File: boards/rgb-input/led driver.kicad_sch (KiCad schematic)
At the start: 4 parts, among them U6 TLC5947DAP

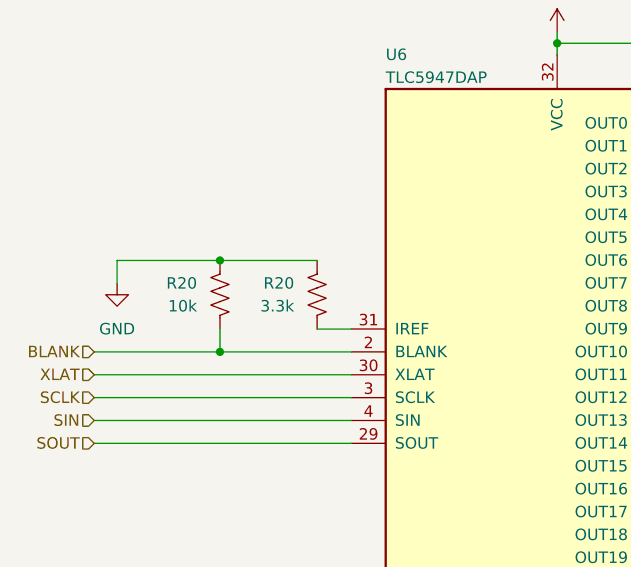
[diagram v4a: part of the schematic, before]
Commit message: routed the rgb setup
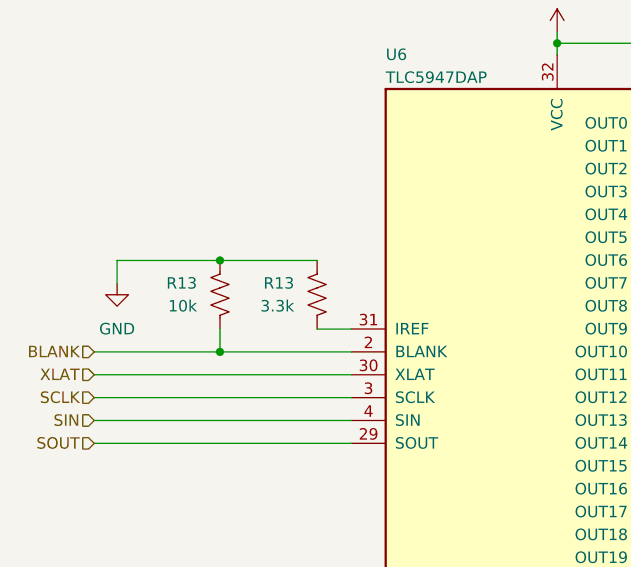
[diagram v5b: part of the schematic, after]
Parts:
- renumbered R20 to R13
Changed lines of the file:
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@@
   (symbol (lib_id "Device:R_US") (at 95.25 80.01 0) (mirror x) (unit 1)
     (in_bom yes) (on_board yes) (dnp no) (fields_autoplaced)
-    (property "Reference" "R20" (at 92.71 78.74 0)
+    (property "Reference" "R13" (at 92.71 78.74 0)
       (effects (font (size 1.27 1.27)) (justify right))
     )
@@
     (instances
       (project "rgb-input"
+        (path "/c83c6236-96e9-46ad-9d7a-9e2efa4a7966/802175d5-fb4b-4457-a117-b0f397189ff7"
+          (reference "R13") (unit 1)
+        )
+        (path "/c83c6236-96e9-46ad-9d7a-9e2efa4a7966/846833bc-7ec6-4ec6-86e7-310fef01b65c/1a23e144-e8e8-4225-b5a6-d9d839ced076"
+          (reference "R46") (unit 1)
+        )
+        (path "/c83c6236-96e9-46ad-9d7a-9e2efa4a7966/846833bc-7ec6-4ec6-86e7-310fef01b65c/720a8c4a-525c-4eec-8216-6ac4d044fce4"
+          (reference "R48") (unit 1)
+        )
+        (path "/c83c6236-96e9-46ad-9d7a-9e2efa4a7966/76149826-8526-4a6c-8e11-6dc0109cc281"
+          (reference "R26") (unit 1)
+        )
+        (path "/c83c6236-96e9-46ad-9d7a-9e2efa4a7966/d24c7443-0875-4d8e-b56e-81b211cd6f3d"
+          (reference "R25") (unit 1)
+        )
+        (path "/c83c6236-96e9-46ad-9d7a-9e2efa4a7966/7fda9512-7a31-4b6e-85db-2478bfe7f375"
+          (reference "R24") (unit 1)
+        )
+        (path "/c83c6236-96e9-46ad-9d7a-9e2efa4a7966/597c781a-3a73-4808-b6ed-8c917478e623"
+          (reference "R23") (unit 1)
+        )
+        (path "/c83c6236-96e9-46ad-9d7a-9e2efa4a7966/1ca70e91-4481-4c96-8c08-39dd142498e5"
+          (reference "R22") (unit 1)
+        )
+        (path "/c83c6236-96e9-46ad-9d7a-9e2efa4a7966/c9e1b2da-9064-45a5-a0a2-ee072f7e1acf"
+          (reference "R21") (unit 1)
+        )
+        (path "/c83c6236-96e9-46ad-9d7a-9e2efa4a7966/ef548cdc-9d5d-4f8e-8f54-0c2e96dbe3f0"
+          (reference "R1") (unit 1)
+        )
         (path "/c83c6236-96e9-46ad-9d7a-9e2efa4a7966/120468c6-3bec-414c-9049-57af589f397a"
           (reference "R20") (unit 1)
-        )
-        (path "/c83c6236-96e9-46ad-9d7a-9e2efa4a7966/846833bc-7ec6-4ec6-86e7-310fef01b65c/1a23e144-e8e8-4225-b5a6-d9d839ced076"
-          (reference "R46") (unit 1)
-        )
-        (path "/c83c6236-96e9-46ad-9d7a-9e2efa4a7966/846833bc-7ec6-4ec6-86e7-310fef01b65c/720a8c4a-525c-4eec-8216-6ac4d044fce4"
-          (reference "R48") (unit 1)
-        )
-        (path "/c83c6236-96e9-46ad-9d7a-9e2efa4a7966/76149826-8526-4a6c-8e11-6dc0109cc281"
-          (reference "R26") (unit 1)
-        )
-        (path "/c83c6236-96e9-46ad-9d7a-9e2efa4a7966/d24c7443-0875-4d8e-b56e-81b211cd6f3d"
-          (reference "R25") (unit 1)
-        )
-        (path "/c83c6236-96e9-46ad-9d7a-9e2efa4a7966/7fda9512-7a31-4b6e-85db-2478bfe7f375"
-          (reference "R24") (unit 1)
-        )
-        (path "/c83c6236-96e9-46ad-9d7a-9e2efa4a7966/597c781a-3a73-4808-b6ed-8c917478e623"
-          (reference "R23") (unit 1)
-        )
-        (path "/c83c6236-96e9-46ad-9d7a-9e2efa4a7966/1ca70e91-4481-4c96-8c08-39dd142498e5"
-          (reference "R22") (unit 1)
-        )
-        (path "/c83c6236-96e9-46ad-9d7a-9e2efa4a7966/c9e1b2da-9064-45a5-a0a2-ee072f7e1acf"
-          (reference "R21") (unit 1)
-        )
-        (path "/c83c6236-96e9-46ad-9d7a-9e2efa4a7966/802175d5-fb4b-4457-a117-b0f397189ff7"
-          (reference "R13") (unit 1)
-        )
-        (path "/c83c6236-96e9-46ad-9d7a-9e2efa4a7966/ef548cdc-9d5d-4f8e-8f54-0c2e96dbe3f0"
-          (reference "R1") (unit 1)
         )
         (path "/c83c6236-96e9-46ad-9d7a-9e2efa4a7966/a581b924-afd8-4b56-b69e-790286072066"
@@
   (symbol (lib_id "Device:R_US") (at 84.455 80.01 0) (mirror x) (unit 1)
     (in_bom yes) (on_board yes) (dnp no) (fields_autoplaced)
-    (property "Reference" "R20" (at 81.915 78.74 0)
+    (property "Reference" "R13" (at 81.915 78.74 0)
       (effects (font (size 1.27 1.27)) (justify right))
     )
@@
     (instances
       (project "rgb-input"
+        (path "/c83c6236-96e9-46ad-9d7a-9e2efa4a7966/802175d5-fb4b-4457-a117-b0f397189ff7"
+          (reference "R13") (unit 1)
+        )
+        (path "/c83c6236-96e9-46ad-9d7a-9e2efa4a7966/846833bc-7ec6-4ec6-86e7-310fef01b65c/1a23e144-e8e8-4225-b5a6-d9d839ced076"
+          (reference "R45") (unit 1)
+        )
+        (path "/c83c6236-96e9-46ad-9d7a-9e2efa4a7966/846833bc-7ec6-4ec6-86e7-310fef01b65c/720a8c4a-525c-4eec-8216-6ac4d044fce4"
+          (reference "R47") (unit 1)
+        )
+        (path "/c83c6236-96e9-46ad-9d7a-9e2efa4a7966/76149826-8526-4a6c-8e11-6dc0109cc281"
+          (reference "R26") (unit 1)
+        )
+        (path "/c83c6236-96e9-46ad-9d7a-9e2efa4a7966/d24c7443-0875-4d8e-b56e-81b211cd6f3d"
+          (reference "R25") (unit 1)
+        )
+        (path "/c83c6236-96e9-46ad-9d7a-9e2efa4a7966/7fda9512-7a31-4b6e-85db-2478bfe7f375"
+          (reference "R24") (unit 1)
+        )
+        (path "/c83c6236-96e9-46ad-9d7a-9e2efa4a7966/597c781a-3a73-4808-b6ed-8c917478e623"
+          (reference "R23") (unit 1)
+        )
+        (path "/c83c6236-96e9-46ad-9d7a-9e2efa4a7966/1ca70e91-4481-4c96-8c08-39dd142498e5"
+          (reference "R22") (unit 1)
+        )
+        (path "/c83c6236-96e9-46ad-9d7a-9e2efa4a7966/c9e1b2da-9064-45a5-a0a2-ee072f7e1acf"
+          (reference "R21") (unit 1)
+        )
+        (path "/c83c6236-96e9-46ad-9d7a-9e2efa4a7966/ef548cdc-9d5d-4f8e-8f54-0c2e96dbe3f0"
+          (reference "R1") (unit 1)
+        )
         (path "/c83c6236-96e9-46ad-9d7a-9e2efa4a7966/120468c6-3bec-414c-9049-57af589f397a"
           (reference "R20") (unit 1)
         )
-        (path "/c83c6236-96e9-46ad-9d7a-9e2efa4a7966/846833bc-7ec6-4ec6-86e7-310fef01b65c/1a23e144-e8e8-4225-b5a6-d9d839ced076"
-          (reference "R45") (unit 1)
-        )
-        (path "/c83c6236-96e9-46ad-9d7a-9e2efa4a7966/846833bc-7ec6-4ec6-86e7-310fef01b65c/720a8c4a-525c-4eec-8216-6ac4d044fce4"
-          (reference "R47") (unit 1)
-        )
-        (path "/c83c6236-96e9-46ad-9d7a-9e2efa4a7966/76149826-8526-4a6c-8e11-6dc0109cc281"
-          (reference "R26") (unit 1)
-        )
-        (path "/c83c6236-96e9-46ad-9d7a-9e2efa4a7966/d24c7443-0875-4d8e-b56e-81b211cd6f3d"
-          (reference "R25") (unit 1)
-        )
-        (path "/c83c6236-96e9-46ad-9d7a-9e2efa4a7966/7fda9512-7a31-4b6e-85db-2478bfe7f375"
-          (reference "R24") (unit 1)
-        )
-        (path "/c83c6236-96e9-46ad-9d7a-9e2efa4a7966/597c781a-3a73-4808-b6ed-8c917478e623"
-          (reference "R23") (unit 1)
-        )
-        (path "/c83c6236-96e9-46ad-9d7a-9e2efa4a7966/1ca70e91-4481-4c96-8c08-39dd142498e5"
-          (reference "R22") (unit 1)
-        )
-        (path "/c83c6236-96e9-46ad-9d7a-9e2efa4a7966/c9e1b2da-9064-45a5-a0a2-ee072f7e1acf"
-          (reference "R21") (unit 1)
-        )
-        (path "/c83c6236-96e9-46ad-9d7a-9e2efa4a7966/802175d5-fb4b-4457-a117-b0f397189ff7"
-          (reference "R13") (unit 1)
-        )
-        (path "/c83c6236-96e9-46ad-9d7a-9e2efa4a7966/ef548cdc-9d5d-4f8e-8f54-0c2e96dbe3f0"
-          (reference "R1") (unit 1)
-        )
         (path "/c83c6236-96e9-46ad-9d7a-9e2efa4a7966/a581b924-afd8-4b56-b69e-790286072066"

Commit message: so much routing.
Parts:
- renumbered C23 to C3, R13 to R1
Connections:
- net GND renamed GNDD

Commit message: various cleanups and tidying
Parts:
- renumbered C3 to C23

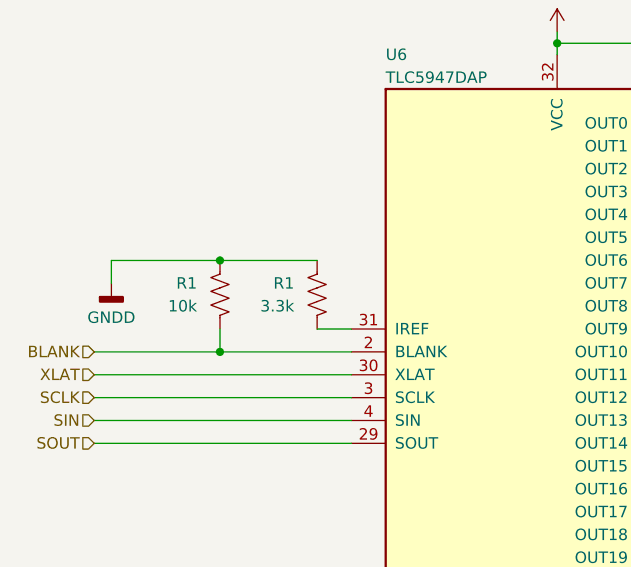
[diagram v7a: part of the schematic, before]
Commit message: rgb input board ready for production too.
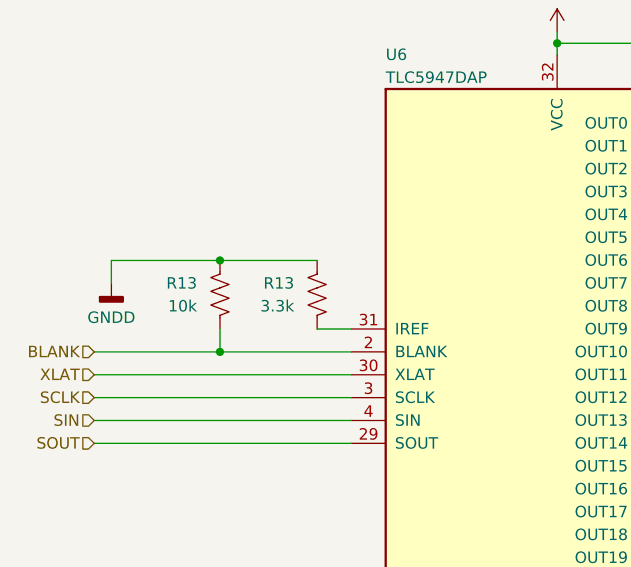
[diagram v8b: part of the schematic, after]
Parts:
- renumbered R1 to R13
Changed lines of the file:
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@@
   (symbol (lib_id "Device:R_US") (at 95.25 80.01 0) (mirror x) (unit 1)
     (in_bom yes) (on_board yes) (dnp no) (fields_autoplaced)
-    (property "Reference" "R1" (at 92.71 78.74 0)
+    (property "Reference" "R13" (at 92.71 78.74 0)
       (effects (font (size 1.27 1.27)) (justify right))
     )
@@
     (instances
       (project "rgb-input"
+        (path "/c83c6236-96e9-46ad-9d7a-9e2efa4a7966/802175d5-fb4b-4457-a117-b0f397189ff7"
+          (reference "R13") (unit 1)
+        )
+        (path "/c83c6236-96e9-46ad-9d7a-9e2efa4a7966/846833bc-7ec6-4ec6-86e7-310fef01b65c/1a23e144-e8e8-4225-b5a6-d9d839ced076"
+          (reference "R46") (unit 1)
+        )
+        (path "/c83c6236-96e9-46ad-9d7a-9e2efa4a7966/846833bc-7ec6-4ec6-86e7-310fef01b65c/720a8c4a-525c-4eec-8216-6ac4d044fce4"
+          (reference "R48") (unit 1)
+        )
+        (path "/c83c6236-96e9-46ad-9d7a-9e2efa4a7966/76149826-8526-4a6c-8e11-6dc0109cc281"
+          (reference "R26") (unit 1)
+        )
+        (path "/c83c6236-96e9-46ad-9d7a-9e2efa4a7966/d24c7443-0875-4d8e-b56e-81b211cd6f3d"
+          (reference "R25") (unit 1)
+        )
+        (path "/c83c6236-96e9-46ad-9d7a-9e2efa4a7966/7fda9512-7a31-4b6e-85db-2478bfe7f375"
+          (reference "R24") (unit 1)
+        )
+        (path "/c83c6236-96e9-46ad-9d7a-9e2efa4a7966/597c781a-3a73-4808-b6ed-8c917478e623"
+          (reference "R23") (unit 1)
+        )
+        (path "/c83c6236-96e9-46ad-9d7a-9e2efa4a7966/1ca70e91-4481-4c96-8c08-39dd142498e5"
+          (reference "R22") (unit 1)
+        )
+        (path "/c83c6236-96e9-46ad-9d7a-9e2efa4a7966/c9e1b2da-9064-45a5-a0a2-ee072f7e1acf"
+          (reference "R21") (unit 1)
+        )
         (path "/c83c6236-96e9-46ad-9d7a-9e2efa4a7966/ef548cdc-9d5d-4f8e-8f54-0c2e96dbe3f0"
           (reference "R1") (unit 1)
         )
-        (path "/c83c6236-96e9-46ad-9d7a-9e2efa4a7966/846833bc-7ec6-4ec6-86e7-310fef01b65c/1a23e144-e8e8-4225-b5a6-d9d839ced076"
-          (reference "R46") (unit 1)
-        )
-        (path "/c83c6236-96e9-46ad-9d7a-9e2efa4a7966/846833bc-7ec6-4ec6-86e7-310fef01b65c/720a8c4a-525c-4eec-8216-6ac4d044fce4"
-          (reference "R48") (unit 1)
-        )
-        (path "/c83c6236-96e9-46ad-9d7a-9e2efa4a7966/76149826-8526-4a6c-8e11-6dc0109cc281"
-          (reference "R26") (unit 1)
-        )
-        (path "/c83c6236-96e9-46ad-9d7a-9e2efa4a7966/d24c7443-0875-4d8e-b56e-81b211cd6f3d"
-          (reference "R25") (unit 1)
-        )
-        (path "/c83c6236-96e9-46ad-9d7a-9e2efa4a7966/7fda9512-7a31-4b6e-85db-2478bfe7f375"
-          (reference "R24") (unit 1)
-        )
-        (path "/c83c6236-96e9-46ad-9d7a-9e2efa4a7966/597c781a-3a73-4808-b6ed-8c917478e623"
-          (reference "R23") (unit 1)
-        )
-        (path "/c83c6236-96e9-46ad-9d7a-9e2efa4a7966/1ca70e91-4481-4c96-8c08-39dd142498e5"
-          (reference "R22") (unit 1)
-        )
-        (path "/c83c6236-96e9-46ad-9d7a-9e2efa4a7966/c9e1b2da-9064-45a5-a0a2-ee072f7e1acf"
-          (reference "R21") (unit 1)
-        )
         (path "/c83c6236-96e9-46ad-9d7a-9e2efa4a7966/120468c6-3bec-414c-9049-57af589f397a"
           (reference "R20") (unit 1)
-        )
-        (path "/c83c6236-96e9-46ad-9d7a-9e2efa4a7966/802175d5-fb4b-4457-a117-b0f397189ff7"
-          (reference "R13") (unit 1)
         )
         (path "/c83c6236-96e9-46ad-9d7a-9e2efa4a7966/a581b924-afd8-4b56-b69e-790286072066"
@@
   (symbol (lib_id "Device:R_US") (at 84.455 80.01 0) (mirror x) (unit 1)
     (in_bom yes) (on_board yes) (dnp no) (fields_autoplaced)
-    (property "Reference" "R1" (at 81.915 78.74 0)
+    (property "Reference" "R13" (at 81.915 78.74 0)
       (effects (font (size 1.27 1.27)) (justify right))
     )
@@
     (instances
       (project "rgb-input"
+        (path "/c83c6236-96e9-46ad-9d7a-9e2efa4a7966/802175d5-fb4b-4457-a117-b0f397189ff7"
+          (reference "R13") (unit 1)
+        )
+        (path "/c83c6236-96e9-46ad-9d7a-9e2efa4a7966/846833bc-7ec6-4ec6-86e7-310fef01b65c/1a23e144-e8e8-4225-b5a6-d9d839ced076"
+          (reference "R45") (unit 1)
+        )
+        (path "/c83c6236-96e9-46ad-9d7a-9e2efa4a7966/846833bc-7ec6-4ec6-86e7-310fef01b65c/720a8c4a-525c-4eec-8216-6ac4d044fce4"
+          (reference "R47") (unit 1)
+        )
+        (path "/c83c6236-96e9-46ad-9d7a-9e2efa4a7966/76149826-8526-4a6c-8e11-6dc0109cc281"
+          (reference "R26") (unit 1)
+        )
+        (path "/c83c6236-96e9-46ad-9d7a-9e2efa4a7966/d24c7443-0875-4d8e-b56e-81b211cd6f3d"
+          (reference "R25") (unit 1)
+        )
+        (path "/c83c6236-96e9-46ad-9d7a-9e2efa4a7966/7fda9512-7a31-4b6e-85db-2478bfe7f375"
+          (reference "R24") (unit 1)
+        )
+        (path "/c83c6236-96e9-46ad-9d7a-9e2efa4a7966/597c781a-3a73-4808-b6ed-8c917478e623"
+          (reference "R23") (unit 1)
+        )
+        (path "/c83c6236-96e9-46ad-9d7a-9e2efa4a7966/1ca70e91-4481-4c96-8c08-39dd142498e5"
+          (reference "R22") (unit 1)
+        )
+        (path "/c83c6236-96e9-46ad-9d7a-9e2efa4a7966/c9e1b2da-9064-45a5-a0a2-ee072f7e1acf"
+          (reference "R21") (unit 1)
+        )
         (path "/c83c6236-96e9-46ad-9d7a-9e2efa4a7966/ef548cdc-9d5d-4f8e-8f54-0c2e96dbe3f0"
           (reference "R1") (unit 1)
         )
-        (path "/c83c6236-96e9-46ad-9d7a-9e2efa4a7966/846833bc-7ec6-4ec6-86e7-310fef01b65c/1a23e144-e8e8-4225-b5a6-d9d839ced076"
-          (reference "R45") (unit 1)
-        )
-        (path "/c83c6236-96e9-46ad-9d7a-9e2efa4a7966/846833bc-7ec6-4ec6-86e7-310fef01b65c/720a8c4a-525c-4eec-8216-6ac4d044fce4"
-          (reference "R47") (unit 1)
-        )
-        (path "/c83c6236-96e9-46ad-9d7a-9e2efa4a7966/76149826-8526-4a6c-8e11-6dc0109cc281"
-          (reference "R26") (unit 1)
-        )
-        (path "/c83c6236-96e9-46ad-9d7a-9e2efa4a7966/d24c7443-0875-4d8e-b56e-81b211cd6f3d"
-          (reference "R25") (unit 1)
-        )
-        (path "/c83c6236-96e9-46ad-9d7a-9e2efa4a7966/7fda9512-7a31-4b6e-85db-2478bfe7f375"
-          (reference "R24") (unit 1)
-        )
-        (path "/c83c6236-96e9-46ad-9d7a-9e2efa4a7966/597c781a-3a73-4808-b6ed-8c917478e623"
-          (reference "R23") (unit 1)
-        )
-        (path "/c83c6236-96e9-46ad-9d7a-9e2efa4a7966/1ca70e91-4481-4c96-8c08-39dd142498e5"
-          (reference "R22") (unit 1)
-        )
-        (path "/c83c6236-96e9-46ad-9d7a-9e2efa4a7966/c9e1b2da-9064-45a5-a0a2-ee072f7e1acf"
-          (reference "R21") (unit 1)
-        )
         (path "/c83c6236-96e9-46ad-9d7a-9e2efa4a7966/120468c6-3bec-414c-9049-57af589f397a"
           (reference "R20") (unit 1)
         )
-        (path "/c83c6236-96e9-46ad-9d7a-9e2efa4a7966/802175d5-fb4b-4457-a117-b0f397189ff7"
-          (reference "R13") (unit 1)
-        )
         (path "/c83c6236-96e9-46ad-9d7a-9e2efa4a7966/a581b924-afd8-4b56-b69e-790286072066"
